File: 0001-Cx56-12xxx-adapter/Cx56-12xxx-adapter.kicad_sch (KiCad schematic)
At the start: 11 parts, among them J1 Conn_01x08_Pin, J2 Conn_01x04_Pin, U1 CC56-12EWA

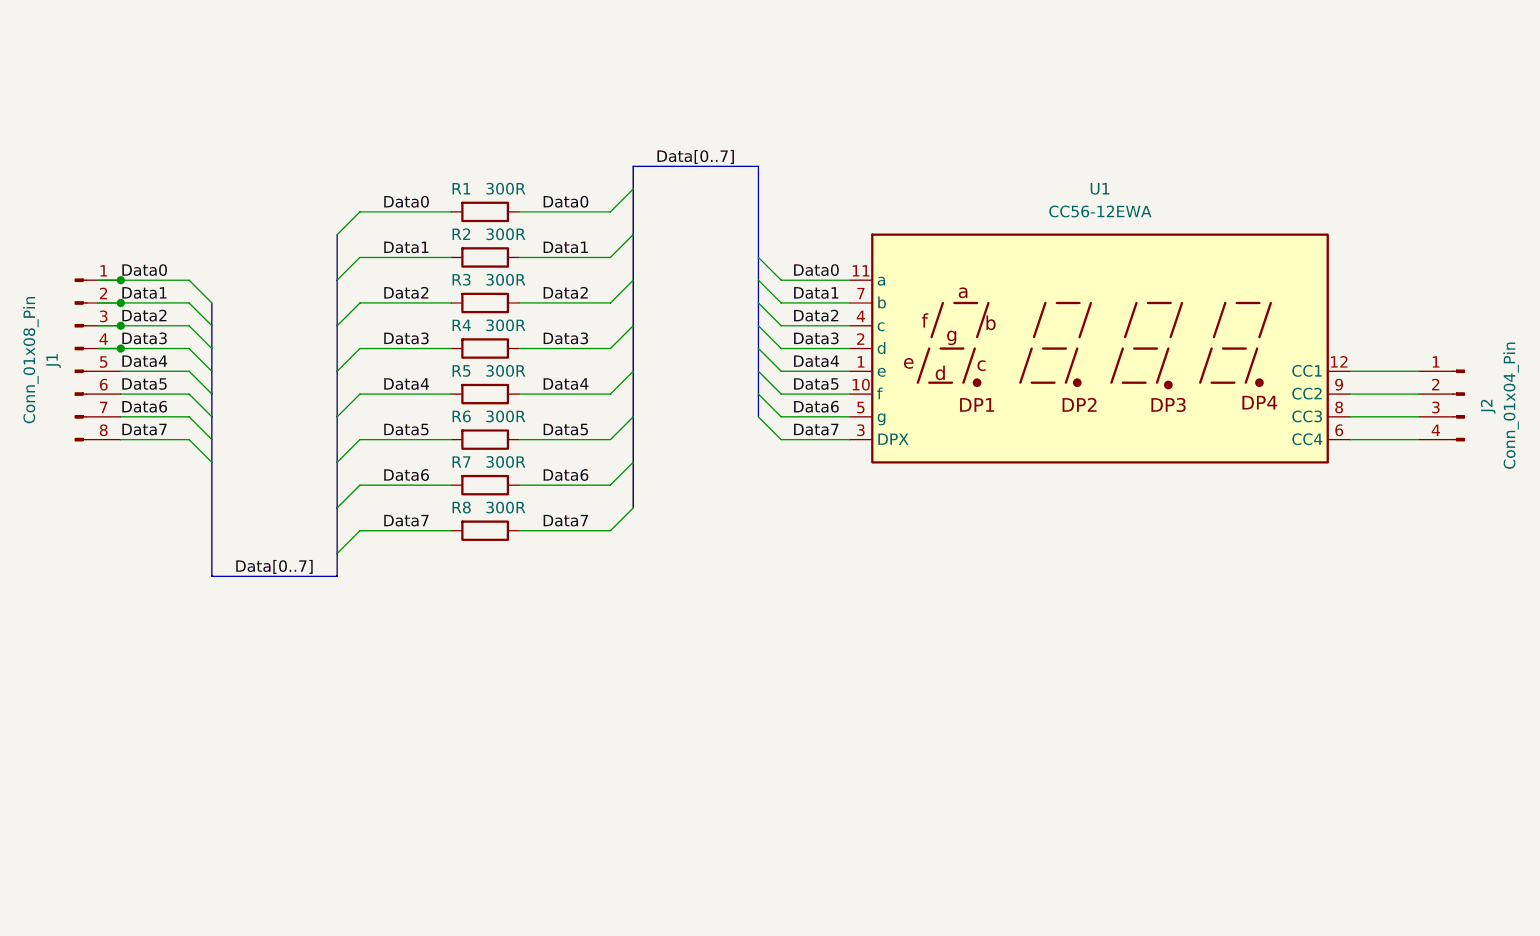
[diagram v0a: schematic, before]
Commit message: Seven-segment display adapter based on CX-12XXX (adjustment)
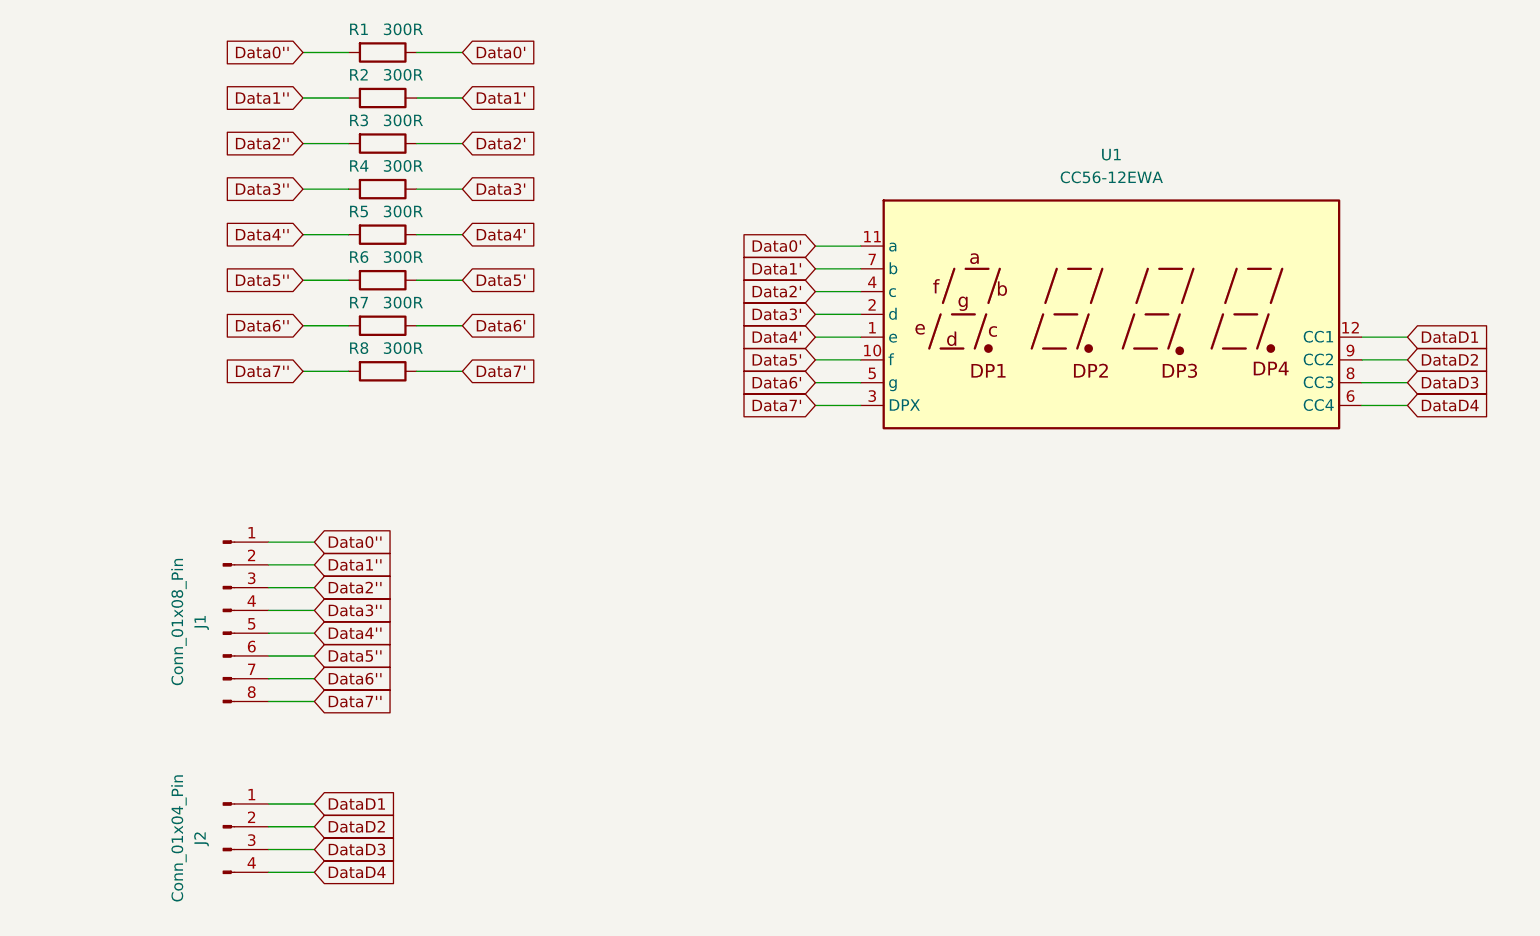
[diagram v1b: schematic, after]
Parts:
- R1, R2, R3, R4, R5, R6, R7, R8: footprint Resistor_THT:R_Axial_DIN0204_L3.6mm_D1.6mm_P7.62mm_Horizontal -> Resistor_SMD:R_0805_2012Metric_Pad1.20x1.40mm_HandSolder
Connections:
- net DataD1: now reaches J2.1 (Pin_1), U1.12 (CC1)
- net DataD2: now reaches J2.2 (Pin_2), U1.9 (CC2)
- net DataD3: now reaches J2.3 (Pin_3), U1.8 (CC3)
- net DataD4: now reaches J2.4 (Pin_4), U1.6 (CC4)
- net Data0 renamed Data0'
- net Data0': no longer J1.1 (Pin_1), R1.2
- net Data1 renamed Data1'
- net Data1': no longer J1.2 (Pin_2), R2.2
- net Data2 renamed Data2'
- net Data2': no longer J1.3 (Pin_3), R3.2
- net Data3 renamed Data3'
- net Data3': no longer J1.4 (Pin_4), R4.2
- net Data4 renamed Data4'
- net Data4': no longer J1.5 (Pin_5), R5.2
- net Data5 renamed Data5'
- net Data5': no longer J1.6 (Pin_6), R6.2
- net Data6 renamed Data6'
- net Data6': no longer J1.7 (Pin_7), R7.2
- net Data7 renamed Data7'
- net Data7': no longer J1.8 (Pin_8), R8.2
- new net Data0'': J1.1 (Pin_1), R1.2
- new net Data1'': J1.2 (Pin_2), R2.2
- new net Data2'': J1.3 (Pin_3), R3.2
- new net Data3'': J1.4 (Pin_4), R4.2
- new net Data4'': J1.5 (Pin_5), R5.2
- new net Data5'': J1.6 (Pin_6), R6.2
- new net Data6'': J1.7 (Pin_7), R7.2
- new net Data7'': J1.8 (Pin_8), R8.2
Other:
- moved on the sheet: J1, J2, R1, R2, R3, R4, R5, R6, R7, R8, U1
